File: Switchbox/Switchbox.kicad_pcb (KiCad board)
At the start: 2 copper layers, 31 parts, among them J1 USB-C_connector, SW1 SW_SPDT, SW2 SW_SPDT, SW3 SW_SPDT, SW4 SW_SPDT, SW5 SW_SPST_LED, SW6 SW_SPDT_BOX, U2 AP63203WU

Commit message: finished all the footprints
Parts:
- added C6: 47µF, switchbox_footprints:CAPC2012X145N, F.Cu at (127.6, 108.3)
- added C7: 0.1 uF, switchbox_footprints:CAPC0603X33N, F.Cu at (124.1, 111.7)
- SW1, SW2, SW3, SW4, SW6: footprint switchbox_footprints:SW_SPDT -> switchbox_footprints:3_pin_header
- SW5: footprint switchbox_footprints:SPST_BUTTON_1190 -> switchbox_footprints:4_pin_header
- moved XBEE1 168.7 mm to (242.0, 124.0), turned to -90 degrees
- moved R7 96.6 mm to (170.9, 116.9), turned to 0 degrees
- moved U2 88.9 mm to (119.7, 116.1)
- moved D6 84.9 mm to (152.1, 131.7)
- moved A2 84.4 mm to (203.5, 94.4), turned to 0 degrees
- moved C1 83.2 mm to (126.9, 111.0)
- moved L1 77.4 mm to (131.2, 107.7), turned to 0 degrees
- moved C3 72.3 mm to (120.0, 108.5)
- moved SW5 66.9 mm to (114.8, 69.3)
- moved R6 65.1 mm to (170.9, 112.8)
- moved D5 61.7 mm to (151.2, 118.0)
- moved C4 58.5 mm to (120.0, 112.0)
- moved C2 58.5 mm to (124.1, 107.8)
- moved C5 58.5 mm to (124.1, 109.7)
- moved R5 49.5 mm to (170.9, 108.8)
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
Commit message: changed LED footprint
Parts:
- moved A2 76.7 mm to (142.1, 48.5), turned to 90 degrees

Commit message: moving around components
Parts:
- moved XBEE1 122.6 mm to (120.0, 111.5)
- moved SW6 116.6 mm to (180.8, 162.9)
- moved J1 97.4 mm to (181.1, 150.6), turned to 180 degrees
- moved R5 75.6 mm to (112.2, 156.5), turned to 90 degrees
- moved R1 70.6 mm to (157.4, 124.5), turned to 90 degrees
- moved R6 68.4 mm to (118.2, 156.5), turned to 90 degrees
- moved R2 67.8 mm to (162.1, 124.5), turned to 90 degrees
- moved R4 67.5 mm to (172.4, 124.5), turned to 90 degrees
- moved R3 66.5 mm to (167.3, 124.5), turned to 90 degrees
- moved C4 66.2 mm to (168.6, 157.0)
- moved C3 65.9 mm to (168.6, 153.0)
- moved D1 64.6 mm to (152.0, 131.0)
- moved A2 63.4 mm to (149.6, 111.5)
- moved D2 62.7 mm to (159.5, 131.0)
- moved D4 62.2 mm to (174.0, 131.0)
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
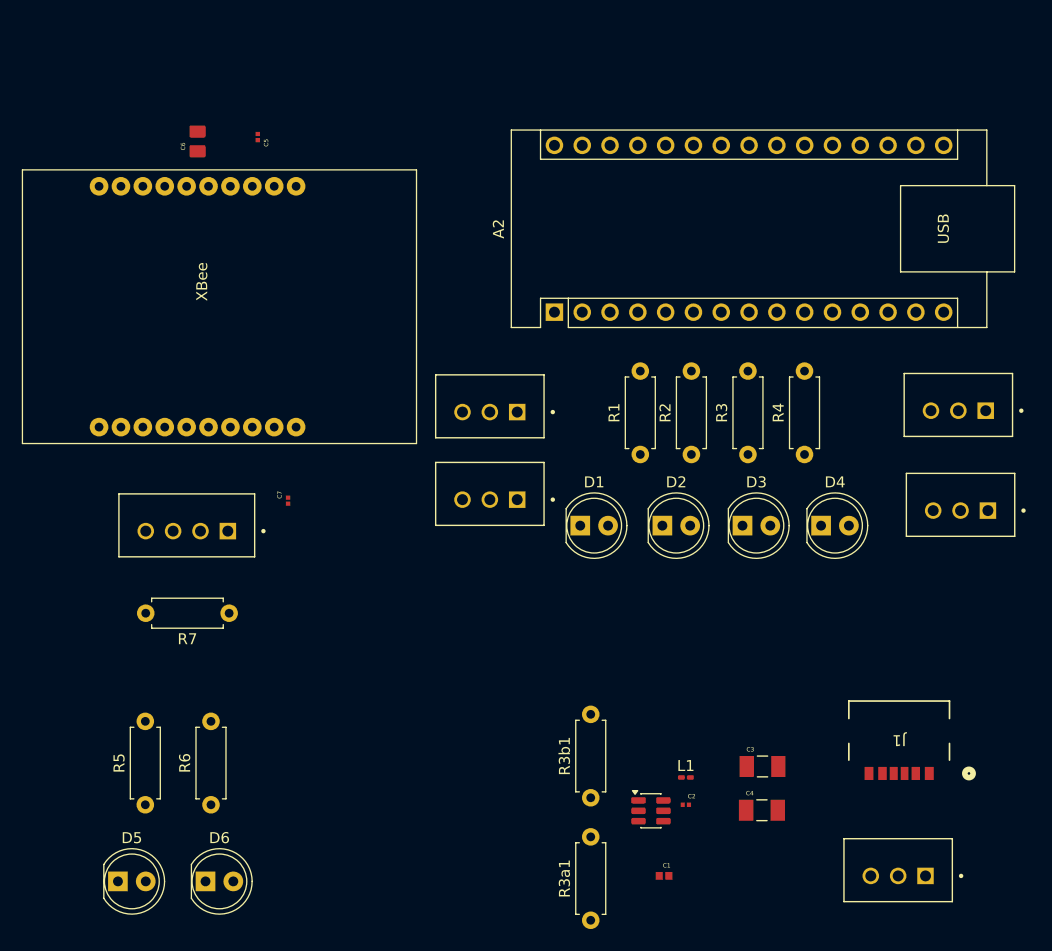
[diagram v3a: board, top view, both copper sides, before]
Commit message: added edge cuts
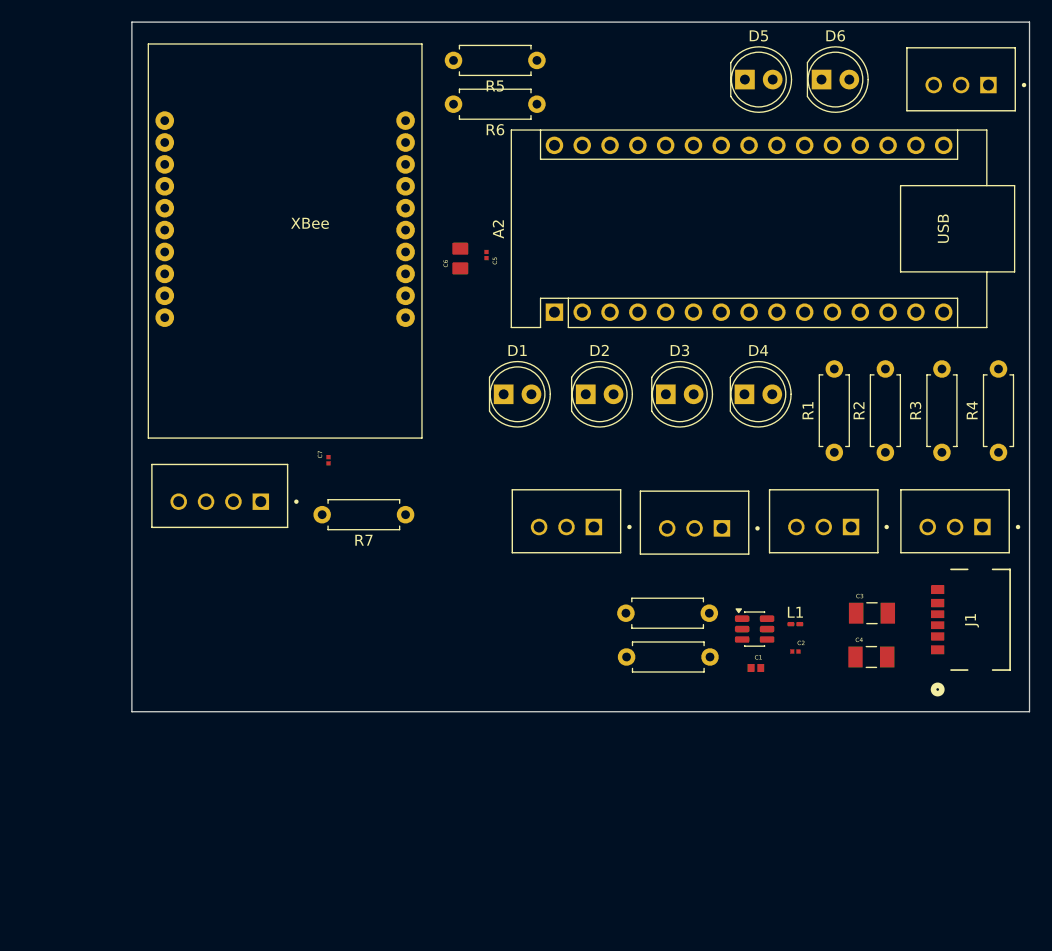
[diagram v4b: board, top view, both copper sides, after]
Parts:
- moved D5 93.0 mm to (167.0, 90.2)
- moved D6 92.4 mm to (174.0, 90.2)
- moved R5 76.8 mm to (148.0, 88.5), turned to 180 degrees
- moved SW6 72.5 mm to (186.6, 90.6)
- moved R6 70.6 mm to (148.0, 92.5), turned to 180 degrees
- moved R3a1 26.4 mm to (163.8, 143.0), turned to 180 degrees
- moved C6 26.3 mm to (141.0, 106.6)
- moved C5 23.5 mm to (143.4, 106.3)
- moved SW2 21.5 mm to (162.2, 131.1)
- moved C1 20.8 mm to (168.0, 144.0)
- moved R3b1 20.0 mm to (163.8, 139.0), turned to 180 degrees
- moved U2 19.1 mm to (167.9, 140.4)
- moved R7 18.5 mm to (136.0, 130.0)
- moved R1 17.7 mm to (175.2, 124.3)
- moved R2 17.7 mm to (179.8, 124.3)
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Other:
- board outline added: 82 x 63 mm

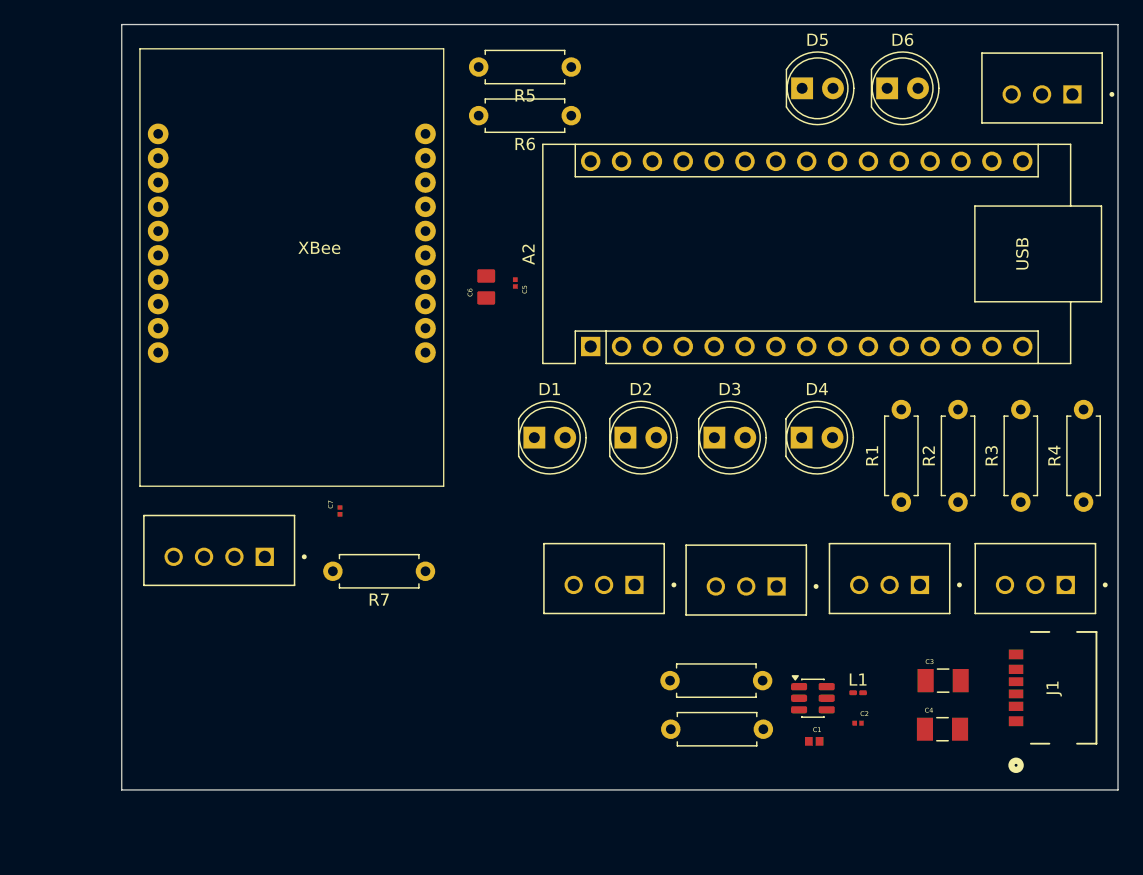
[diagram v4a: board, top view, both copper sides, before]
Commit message: added edge cuts + mounting holes
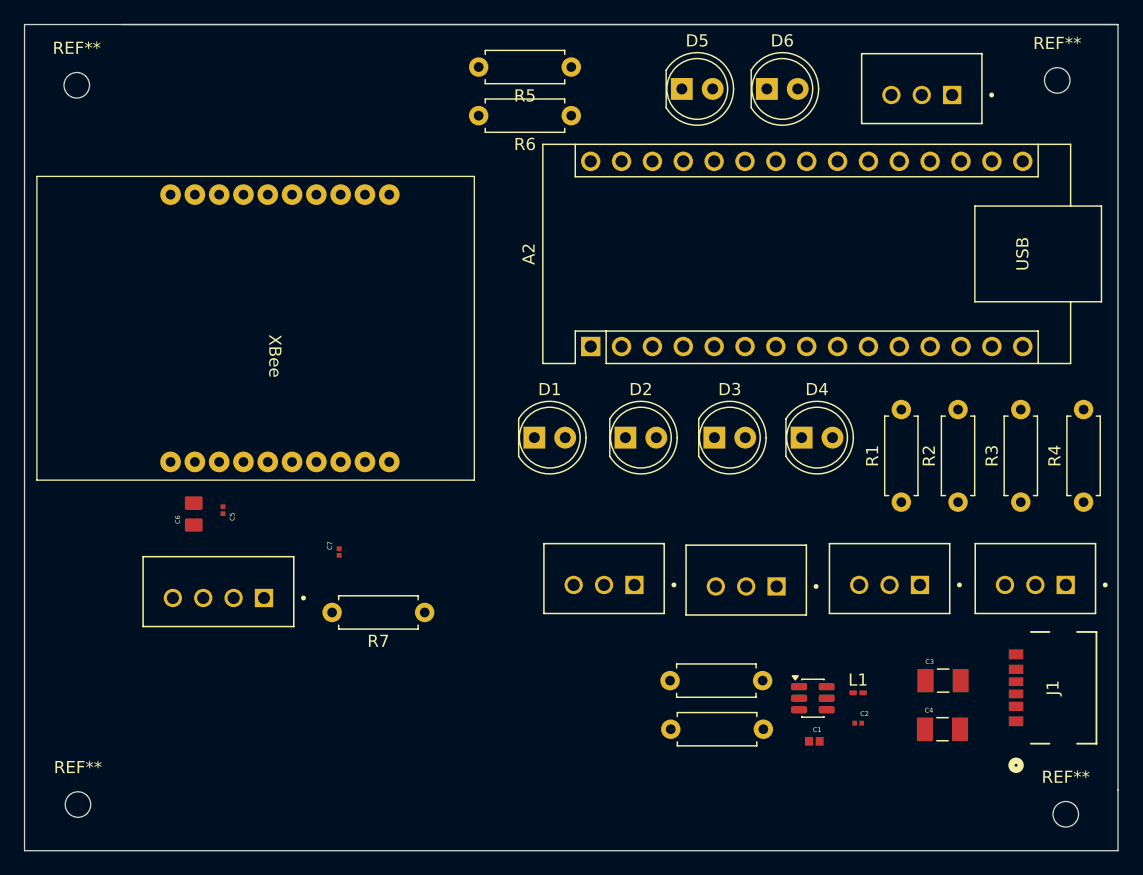
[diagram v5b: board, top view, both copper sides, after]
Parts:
- added REF**: MountingHole_2.1mm, MountingHole:MountingHole_2.1mm, F.Cu at (188.7, 150.0)
- added REF**: MountingHole_2.1mm, MountingHole:MountingHole_2.1mm, F.Cu at (107.3, 90.0)
- added REF**: MountingHole_2.1mm, MountingHole:MountingHole_2.1mm, F.Cu at (188.0, 89.6)
- added REF**: MountingHole_2.1mm, MountingHole:MountingHole_2.1mm, F.Cu at (107.4, 149.2)
- moved C5 30.5 mm to (119.3, 125.0)
- moved C6 30.5 mm to (116.9, 125.3)
- moved D5 9.90 mm to (157.1, 90.3)
- moved D6 9.90 mm to (164.1, 90.3)
- moved SW6 9.90 mm to (176.7, 90.7)
- moved XBEE1 4.94 mm to (121.0, 109.5), turned to 90 degrees
- moved C7 3.39 mm to (128.9, 128.4)
- moved SW5 3.39 mm to (119.0, 132.1)
- moved R7 3.39 mm to (135.9, 133.4)
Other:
- board size 82 x 63 mm -> 90 x 68 mm

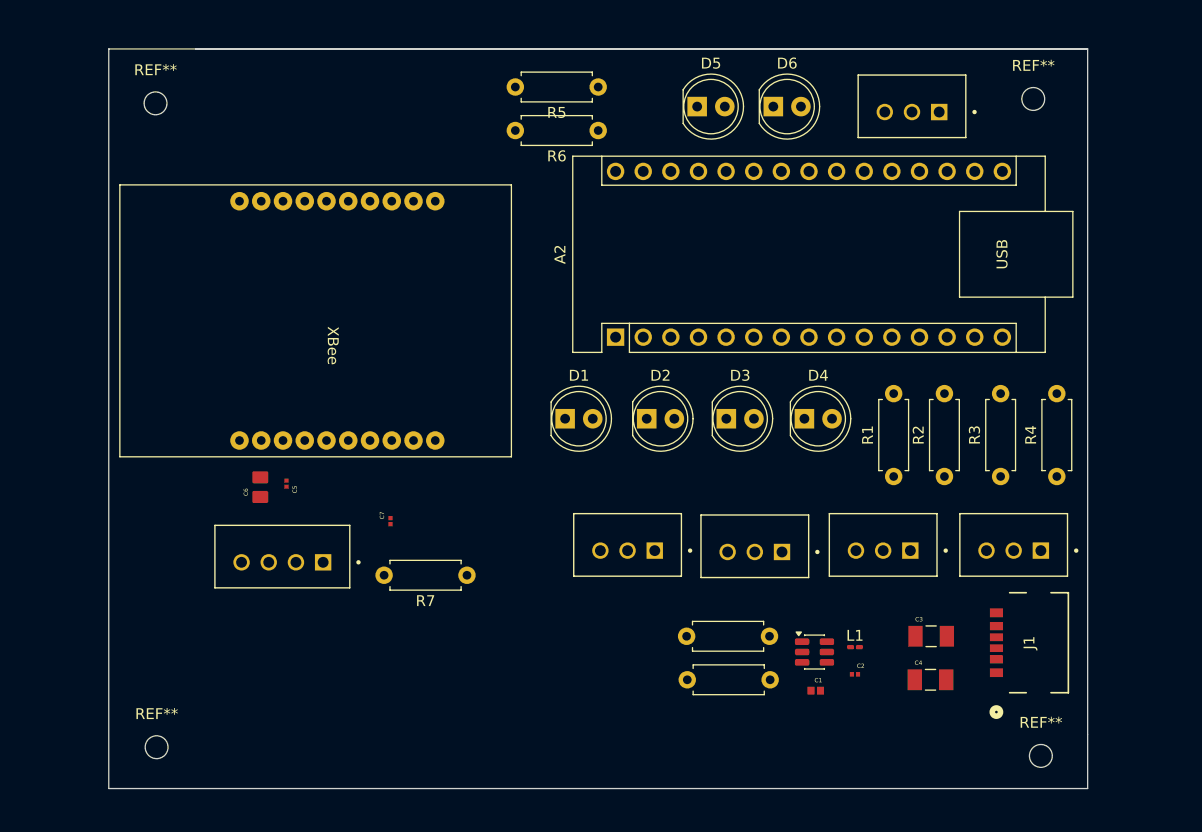
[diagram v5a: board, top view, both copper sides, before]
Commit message: added all but ground traces
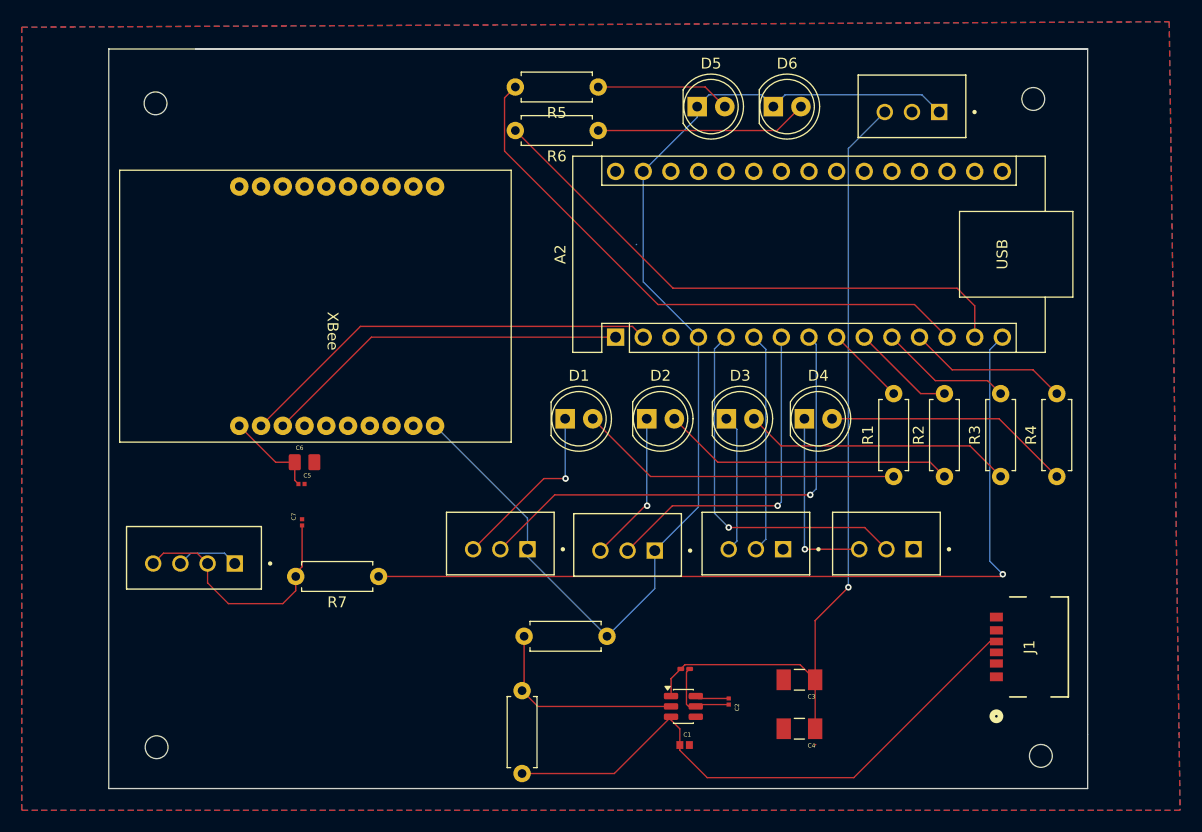
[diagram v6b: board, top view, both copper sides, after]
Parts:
- moved R3a1 22.8 mm to (141.0, 144.0), turned to -90 degrees
- moved R3b1 22.6 mm to (141.2, 139.0), turned to 0 degrees
- moved L1 15.7 mm to (156.0, 142.0), turned to 180 degrees
- moved C1 13.0 mm to (155.9, 149.0)
- moved U2 13.0 mm to (155.8, 145.4)
- moved C4 12.9 mm to (166.5, 147.5), turned to 180 degrees
- moved C3 12.8 mm to (166.5, 143.0), turned to 180 degrees
- moved C2 11.9 mm to (160.0, 145.0), turned to -90 degrees
- moved SW1 11.7 mm to (138.8, 130.9)
- moved SW2 11.7 mm to (150.5, 131.0)
- moved SW3 11.7 mm to (162.3, 130.9)
- moved SW4 11.7 mm to (174.3, 130.9)
- moved C7 8.13 mm to (120.8, 128.5)
- moved R7 8.13 mm to (127.8, 133.5)
- moved SW5 8.13 mm to (110.9, 132.2)
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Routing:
- net GND: track 0.00 -> 112.3 mm
- net BUTTON: track 0.00 -> 80.2 mm, vias 0 -> 1
- net 3.3VBuck: track 0.00 -> 75.4 mm, vias 0 -> 1
- net Sys_Vin: track 0.00 -> 54.6 mm
- net LED5_PWR: track 0.00 -> 54.1 mm
- net LED6_PWR: track 0.00 -> 51.8 mm
- net LED1_STATE: track 0.00 -> 45.6 mm, vias 0 -> 1
- net FROM_XBEE: track 0.00 -> 39.3 mm
- net TO_XBEE: track 0.00 -> 34.0 mm
- net LED4_STATE: track 0.00 -> 33.8 mm, vias 0 -> 1
- net LED2_STATE: track 0.00 -> 31.1 mm, vias 0 -> 1
- net Net-(D1-A): track 0.00 -> 29.9 mm
- net Net-(D2-A): track 0.00 -> 27.0 mm
- net Net-(D3-A): track 0.00 -> 24.9 mm
- net Net-(SW5-A): track 0.00 -> 23.2 mm
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- added copper zone on B.Cu, net GND
- added copper zone on F.Cu, net GND
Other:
- board text added: "${REFERENCE}"

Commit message: possibly finished traces??
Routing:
- net GND: track 112.3 -> 215.0 mm, vias 0 -> 3
- net BOX_STATE: track 9.47 -> 98.9 mm, vias 0 -> 2
